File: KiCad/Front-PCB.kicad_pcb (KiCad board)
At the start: 2 copper layers, 101.6 x 88.9 mm, 23 parts, among them J1 HLW20R-2C7LF, P1 Mounting Vias, P2 CONN_01X01, P3 CONN_01X01, P4 CONN_01X01, U1 MAX7219, U2 LTC-4727JR

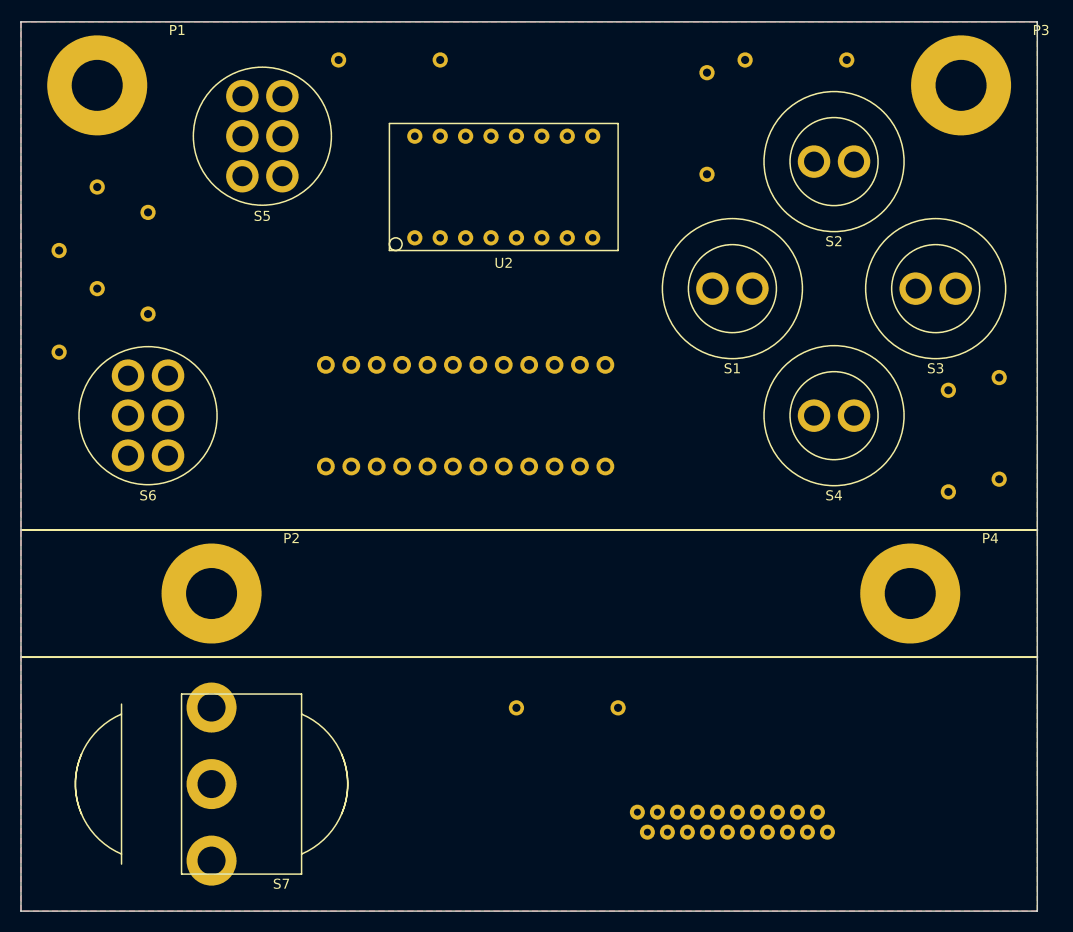
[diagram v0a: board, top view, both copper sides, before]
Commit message: front panel pcb routing complete
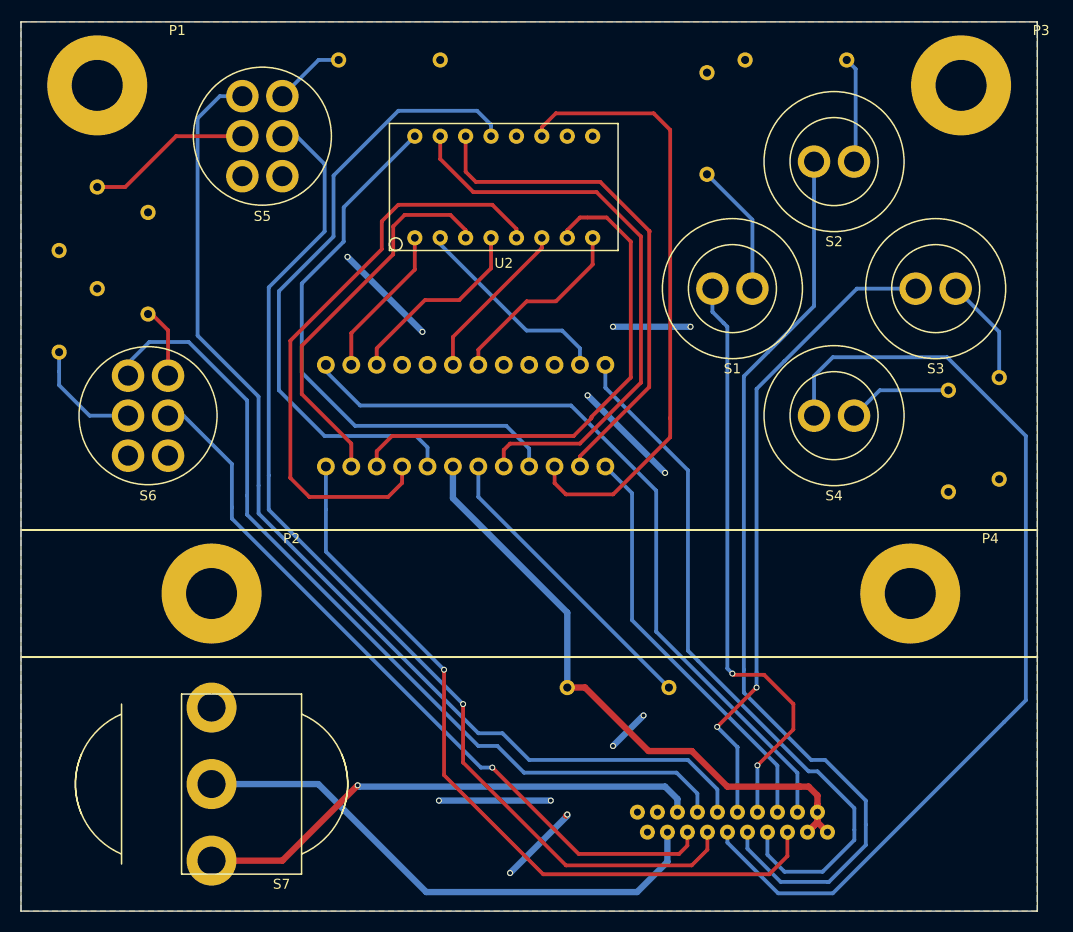
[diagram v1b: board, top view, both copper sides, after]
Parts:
- moved R19 5.47 mm to (135.9, 111.0)
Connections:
- net Net-(J1-Pad10) renamed /right
- net Net-(J1-Pad11) renamed /down
- net Net-(J1-Pad13) renamed /green
- net Net-(J1-Pad15) renamed /red
- net Net-(J1-Pad16) renamed /door1
- net Net-(J1-Pad17) renamed /door2
- net Net-(J1-Pad4) renamed /MOSI
- net Net-(J1-Pad5) renamed /MISO
- net Net-(J1-Pad6) renamed /spiclk
- net Net-(J1-Pad7) renamed /slave
- net Net-(J1-Pad8) renamed /left
- net Net-(J1-Pad9) renamed /up
- net Net-(R19-Pad2) renamed /iset
- net Net-(U1-Pad11) renamed /dig2
- net Net-(U1-Pad2) renamed /dig1
- net Net-(U1-Pad3) renamed /dig4
- net Net-(U1-Pad6) renamed /dig5
- net Net-(U1-Pad7) renamed /dig3
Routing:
- net Net-(J1-Pad12): track 0.00 -> 107.0 mm
- net /green: track 0.00 -> 106.6 mm, vias 0 -> 1
- net /down: track 0.00 -> 96.6 mm
- net /up: track 0.00 -> 93.5 mm
- net Net-(J1-Pad14): track 0.00 -> 86.3 mm
- net /MISO: track 0.00 -> 77.3 mm, vias 0 -> 1
- net /MOSI: track 0.00 -> 76.6 mm
- net /red: track 0.00 -> 75.0 mm, vias 0 -> 1
- net /slave: track 0.00 -> 71.3 mm
- net /right: track 0.00 -> 64.9 mm, vias 0 -> 2
- net +5V: track 0.00 -> 64.2 mm
- net Net-(U1-Pad20): track 0.00 -> 63.0 mm
- net Net-(U1-Pad15): track 0.00 -> 61.8 mm
- net Net-(U1-Pad21): track 0.00 -> 59.7 mm
- net /left: track 0.00 -> 59.0 mm, vias 0 -> 2
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
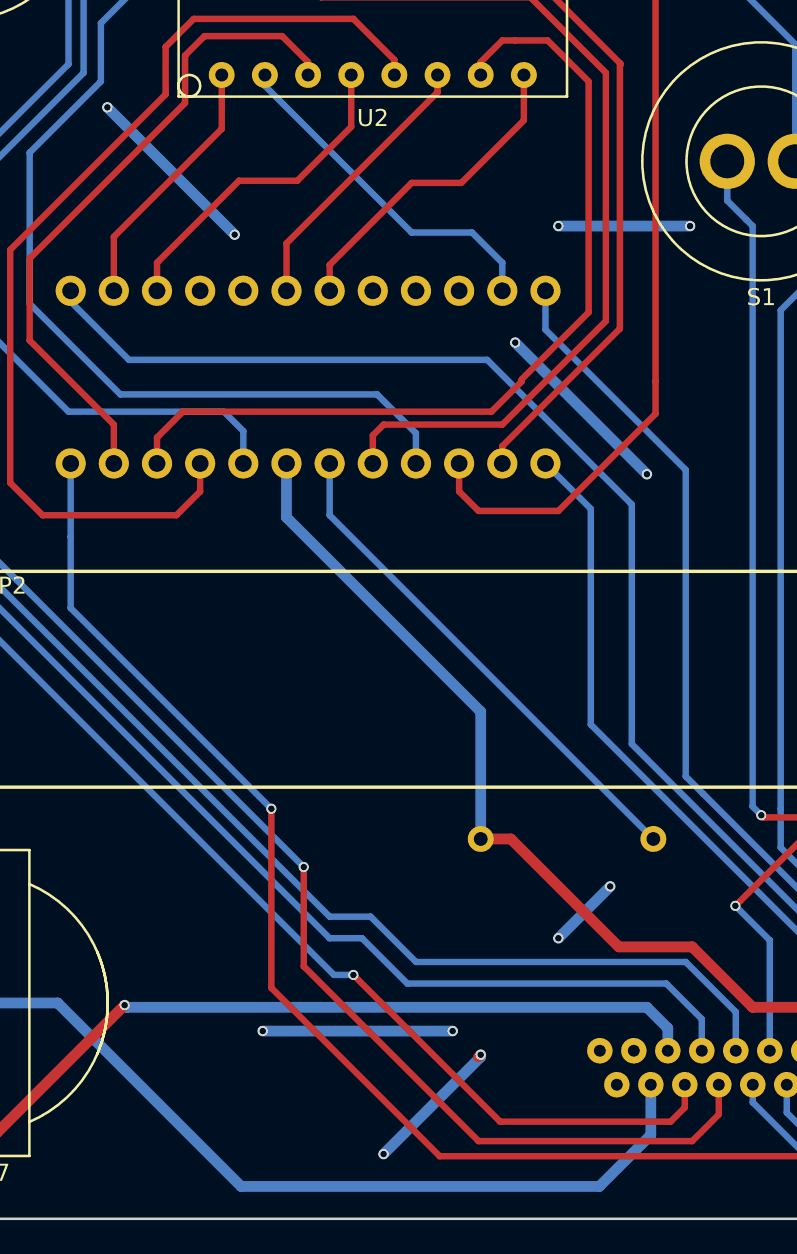
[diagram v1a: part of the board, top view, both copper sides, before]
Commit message: nichrome mounting parts added to bom and feedback terminal block removed
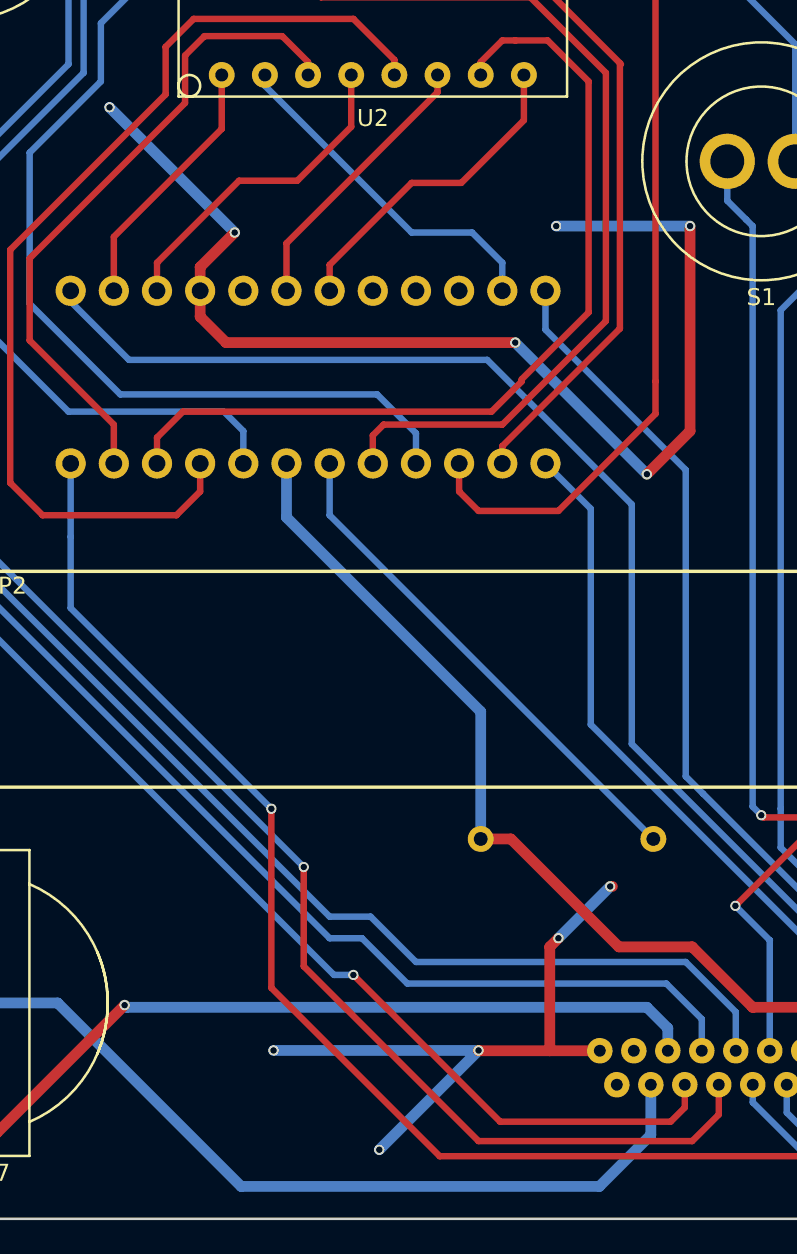
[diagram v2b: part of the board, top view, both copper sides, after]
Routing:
- net GND: track 0.00 -> 108.6 mm, vias 0 -> 11
- net (no net): track 53.2 -> 0.00 mm, vias 12 -> 0
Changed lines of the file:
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@@
   (general
     (links 56)
-    (no_connects 1)
-    (area 76.124999 44.374999 177.875001 133.425001)
+    (no_connects 0)
+    (area 76.099999 42.621 179.485191 133.425001)
     (thickness 1.6)
-    (drawings 6)
-    (tracks 306)
+    (drawings 10)
+    (tracks 316)
     (zones 0)
     (modules 23)
@@
     (visible_elements FFFFFF7F)
     (pcbplotparams
-      (layerselection 0x00030_80000001)
+      (layerselection 0x010e0_80000001)
       (usegerberextensions false)
       (excludeedgelayer true)
@@
       (outputformat 1)
       (mirror false)
-      (drillshape 1)
+      (drillshape 0)
       (scaleselection 1)
-      (outputdirectory ""))
+      (outputdirectory Gerbers/))
   )
   (net 0 "")
@@
       (net 4 GND))
   )
+  (dimension 12.7 (width 0.3) (layer Dwgs.User)
+    (gr_text "0.5000 in" (at 60.880001 101.6 270) (layer Dwgs.User)
+      (effects (font (size 1.5 1.5) (thickness 0.3)))
+    )
+    (feature1 (pts (xy 76.2 107.95) (xy 59.530001 107.95)))
+    (feature2 (pts (xy 76.2 95.25) (xy 59.530001 95.25)))
+    (crossbar (pts (xy 62.230001 95.25) (xy 62.230001 107.95)))
+    (arrow1a (pts (xy 62.230001 107.95) (xy 61.64358 106.823496)))
+    (arrow1b (pts (xy 62.230001 107.95) (xy 62.816422 106.823496)))
+    (arrow2a (pts (xy 62.230001 95.25) (xy 61.64358 96.376504)))
+    (arrow2b (pts (xy 62.230001 95.25) (xy 62.816422 96.376504)))
+  )
+  (dimension 19.05 (width 0.3) (layer Dwgs.User)
+    (gr_text "0.7500 in" (at 85.725 138.51) (layer Dwgs.User)
+      (effects (font (size 1.5 1.5) (thickness 0.3)))
+    )
+    (feature1 (pts (xy 76.2 101.6) (xy 76.2 139.86)))
+    (feature2 (pts (xy 95.25 101.6) (xy 95.25 139.86)))
+    (crossbar (pts (xy 95.25 137.16) (xy 76.2 137.16)))
+    (arrow1a (pts (xy 76.2 137.16) (xy 77.326504 136.573579)))
+    (arrow1b (pts (xy 76.2 137.16) (xy 77.326504 137.746421)))
+    (arrow2a (pts (xy 95.25 137.16) (xy 94.123496 136.573579)))
+    (arrow2b (pts (xy 95.25 137.16) (xy 94.123496 137.746421)))
+  )
+  (dimension 88.9 (width 0.3) (layer Dwgs.User)
+    (gr_text "3.5000 in" (at 203.026 88.9 270) (layer Dwgs.User)
+      (effects (font (size 1.5 1.5) (thickness 0.3)))
+    )
+    (feature1 (pts (xy 177.8 133.35) (xy 204.376 133.35)))
+    (feature2 (pts (xy 177.8 44.45) (xy 204.376 44.45)))
+    (crossbar (pts (xy 201.676 44.45) (xy 201.676 133.35)))
+    (arrow1a (pts (xy 201.676 133.35) (xy 201.089579 132.223496)))
+    (arrow1b (pts (xy 201.676 133.35) (xy 202.262421 132.223496)))
+    (arrow2a (pts (xy 201.676 44.45) (xy 201.089579 45.576504)))
+    (arrow2b (pts (xy 201.676 44.45) (xy 202.262421 45.576504)))
+  )
+  (dimension 101.6 (width 0.3) (layer Dwgs.User)
+    (gr_text "4.0000 in" (at 127 144.605999) (layer Dwgs.User)
+      (effects (font (size 1.5 1.5) (thickness 0.3)))
+    )
+    (feature1 (pts (xy 177.8 133.35) (xy 177.8 145.955999)))
+    (feature2 (pts (xy 76.2 133.35) (xy 76.2 145.955999)))
+    (crossbar (pts (xy 76.2 143.255999) (xy 177.8 143.255999)))
+    (arrow1a (pts (xy 177.8 143.255999) (xy 176.673496 143.84242)))
+    (arrow1b (pts (xy 177.8 143.255999) (xy 176.673496 142.669578)))
+    (arrow2a (pts (xy 76.2 143.255999) (xy 77.326504 143.84242)))
+    (arrow2b (pts (xy 76.2 143.255999) (xy 77.326504 142.669578)))
+  )
   (gr_line (start 76.2 44.45) (end 177.8 44.45) (angle 90) (layer Edge.Cuts) (width 0.15))
   (gr_line (start 76.2 133.35) (end 177.8 133.35) (angle 90) (layer Edge.Cuts) (width 0.15))
@@
   (gr_line (start 177.8 44.45) (end 177.8 133.35) (angle 90) (layer Edge.Cuts) (width 0.15))
   (gr_line (start 76.2 44.45) (end 76.2 133.35) (angle 90) (layer Edge.Cuts) (width 0.15))
-  (via (at 125.095 129.54) (size 0.6) (drill 0.381) (layers F.Cu B.Cu) (net 0))
-  (segment (start 130.683 123.825) (end 130.81 123.698) (width 0.635) (layer F.Cu) (net 0))
-  (via (at 130.81 123.698) (size 0.6) (drill 0.381) (layers F.Cu B.Cu) (net 0))
-  (segment (start 130.81 123.825) (end 130.81 123.698) (width 0.635) (layer B.Cu) (net 0))
-  (segment (start 130.81 123.825) (end 125.095 129.54) (width 0.635) (layer B.Cu) (net 0))
-  (via (at 129.159 122.301) (size 0.6) (drill 0.381) (layers F.Cu B.Cu) (net 0))
-  (via (at 117.983 122.301) (size 0.6) (drill 0.381) (layers F.Cu B.Cu) (net 0))
-  (segment (start 129.159 122.301) (end 117.983 122.301) (width 0.635) (layer B.Cu) (net 0))
-  (via (at 135.382 74.93) (size 0.6) (drill 0.381) (layers F.Cu B.Cu) (net 0))
-  (via (at 143.129 74.93) (size 0.6) (drill 0.381) (layers F.Cu B.Cu) (net 0))
-  (segment (start 135.382 74.93) (end 143.129 74.93) (width 0.635) (layer B.Cu) (net 0))
-  (via (at 132.842 81.788) (size 0.6) (drill 0.381) (layers F.Cu B.Cu) (net 0))
-  (via (at 140.589 89.535) (size 0.6) (drill 0.381) (layers F.Cu B.Cu) (net 0))
-  (segment (start 132.842 81.788) (end 140.589 89.535) (width 0.635) (layer B.Cu) (net 0))
-  (via (at 116.332 75.438) (size 0.6) (drill 0.381) (layers F.Cu B.Cu) (net 0))
-  (via (at 108.839 67.945) (size 0.6) (drill 0.381) (layers F.Cu B.Cu) (net 0))
-  (segment (start 116.332 75.438) (end 108.839 67.945) (width 0.635) (layer B.Cu) (net 0))
-  (via (at 135.382 116.84) (size 0.6) (drill 0.381) (layers F.Cu B.Cu) (net 0))
-  (via (at 138.43 113.792) (size 0.6) (drill 0.381) (layers F.Cu B.Cu) (net 0))
-  (segment (start 135.382 116.84) (end 138.43 113.792) (width 0.635) (layer B.Cu) (net 0))
   (segment (start 154.051 120.904) (end 154.94 120.904) (width 0.635) (layer F.Cu) (net 1))
   (segment (start 155.82 124.46) (end 155.82 122.673) (width 0.635) (layer F.Cu) (net 1))
@@
   (segment (start 98.806 93.726) (end 121.92 116.84) (width 0.381) (layer B.Cu) (net 3))
   (segment (start 86.9 79.82) (end 86.9 78.581) (width 0.381) (layer B.Cu) (net 3))
+  (segment (start 114.3 78.74) (end 114.3 77.343) (width 0.635) (layer F.Cu) (net 4) (status 400000))
+  (via (at 108.966 67.945) (size 0.6) (drill 0.381) (layers F.Cu B.Cu) (net 4))
+  (segment (start 116.332 75.311) (end 108.966 67.945) (width 0.635) (layer B.Cu) (net 4))
+  (via (at 116.332 75.311) (size 0.6) (drill 0.381) (layers F.Cu B.Cu) (net 4))
+  (segment (start 114.3 77.343) (end 116.332 75.311) (width 0.635) (layer F.Cu) (net 4))
+  (segment (start 114.3 78.74) (end 114.3 80.264) (width 0.635) (layer F.Cu) (net 4) (status 400000))
+  (via (at 135.255 74.93) (size 0.6) (drill 0.381) (layers F.Cu B.Cu) (net 4))
+  (segment (start 143.129 74.93) (end 135.255 74.93) (width 0.635) (layer B.Cu) (net 4))
+  (via (at 143.129 74.93) (size 0.6) (drill 0.381) (layers F.Cu B.Cu) (net 4))
+  (segment (start 143.129 86.995) (end 143.129 74.93) (width 0.635) (layer F.Cu) (net 4))
+  (segment (start 140.589 89.535) (end 143.129 86.995) (width 0.635) (layer F.Cu) (net 4))
+  (via (at 140.589 89.535) (size 0.6) (drill 0.381) (layers F.Cu B.Cu) (net 4))
+  (segment (start 132.842 81.788) (end 140.589 89.535) (width 0.635) (layer B.Cu) (net 4))
+  (via (at 132.842 81.788) (size 0.6) (drill 0.381) (layers F.Cu B.Cu) (net 4))
+  (segment (start 115.824 81.788) (end 132.842 81.788) (width 0.635) (layer F.Cu) (net 4))
+  (segment (start 114.3 80.264) (end 115.824 81.788) (width 0.635) (layer F.Cu) (net 4))
+  (segment (start 134.874 123.46) (end 134.874 117.348) (width 0.635) (layer F.Cu) (net 4))
+  (segment (start 138.43 113.792) (end 138.557 113.792) (width 0.635) (layer F.Cu) (net 4))
+  (via (at 138.43 113.792) (size 0.6) (drill 0.381) (layers F.Cu B.Cu) (net 4))
+  (segment (start 135.382 116.84) (end 138.43 113.792) (width 0.635) (layer B.Cu) (net 4))
+  (via (at 135.382 116.84) (size 0.6) (drill 0.381) (layers F.Cu B.Cu) (net 4))
+  (segment (start 134.874 117.348) (end 135.382 116.84) (width 0.635) (layer F.Cu) (net 4))
+  (segment (start 130.683 123.444) (end 124.841 129.286) (width 0.635) (layer B.Cu) (net 4))
+  (via (at 124.841 129.286) (size 0.6) (drill 0.381) (layers F.Cu B.Cu) (net 4))
+  (segment (start 137.82 123.46) (end 134.874 123.46) (width 0.635) (layer F.Cu) (net 4) (status 400000))
+  (segment (start 134.874 123.46) (end 130.699 123.46) (width 0.635) (layer F.Cu) (net 4))
+  (via (at 118.618 123.444) (size 0.6) (drill 0.381) (layers F.Cu B.Cu) (net 4))
+  (segment (start 130.683 123.444) (end 118.618 123.444) (width 0.635) (layer B.Cu) (net 4))
+  (via (at 130.683 123.444) (size 0.6) (drill 0.381) (layers F.Cu B.Cu) (net 4))
+  (segment (start 130.699 123.46) (end 130.683 123.444) (width 0.635) (layer F.Cu) (net 4))
   (segment (start 149.32 71.12) (end 149.32 64.23) (width 0.381) (layer B.Cu) (net 5))
   (segment (start 149.32 64.23) (end 144.78 59.69) (width 0.381) (layer B.Cu) (net 5))
